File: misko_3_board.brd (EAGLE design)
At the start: 337 x 187 mm, 171 parts, among them IC1 ATMEGA1281-16AU, IC10 ORG1510-MK4, IC11 TPS3808G33DBVT, IC12 LTC4425, IC13 RN-42, IC14 ADXL345, IC15 74HCT1G32, IC16 FM25W256-SOIC, IC17 MICROSD_SPI_MODE, IC18 FH12-30S-0.5SH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

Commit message: - corrected too big spatial dimensions (took 1mm off), rerouted what needed to be rerouted, ERC & DRC are error free
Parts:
- moved CONN13 139.2 mm to (216.0, 13.0)
- moved LED1 139.2 mm to (210.0, 17.0)
- moved LED2 139.2 mm to (210.0, 13.5)
- moved LED5 139.2 mm to (225.5, 16.8)
- moved LED6 139.2 mm to (225.5, 13.5)
- moved R41 139.2 mm to (229.5, 13.5)
- moved R50 139.2 mm to (220.2, 13.5)
- moved S4 139.2 mm to (225.5, 8.50)
- moved S5 139.2 mm to (207.5, 8.50)
- moved C1 131.7 mm to (108.5, 32.6)
- moved C10 131.7 mm to (164.5, 2.50)
- moved C12 131.7 mm to (131.7, 23.5)
- moved C15 131.7 mm to (106.5, 8.50)
- moved C16 131.7 mm to (122.5, 23.5)
- moved C2 131.7 mm to (150.5, 21.0)
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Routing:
- net VUSB: track 47.1 -> 12.1 mm, vias 0 -> 1
- net RESET: track 167.0 -> 163.8 mm
- net VCC: track 458.7 -> 457.2 mm
- net GSM_ANT: track 11.0 -> 10.4 mm
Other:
- board size 337 x 187 mm -> 233 x 140 mm
- board text added: "Miško v.1"
- board text removed: "Miško"

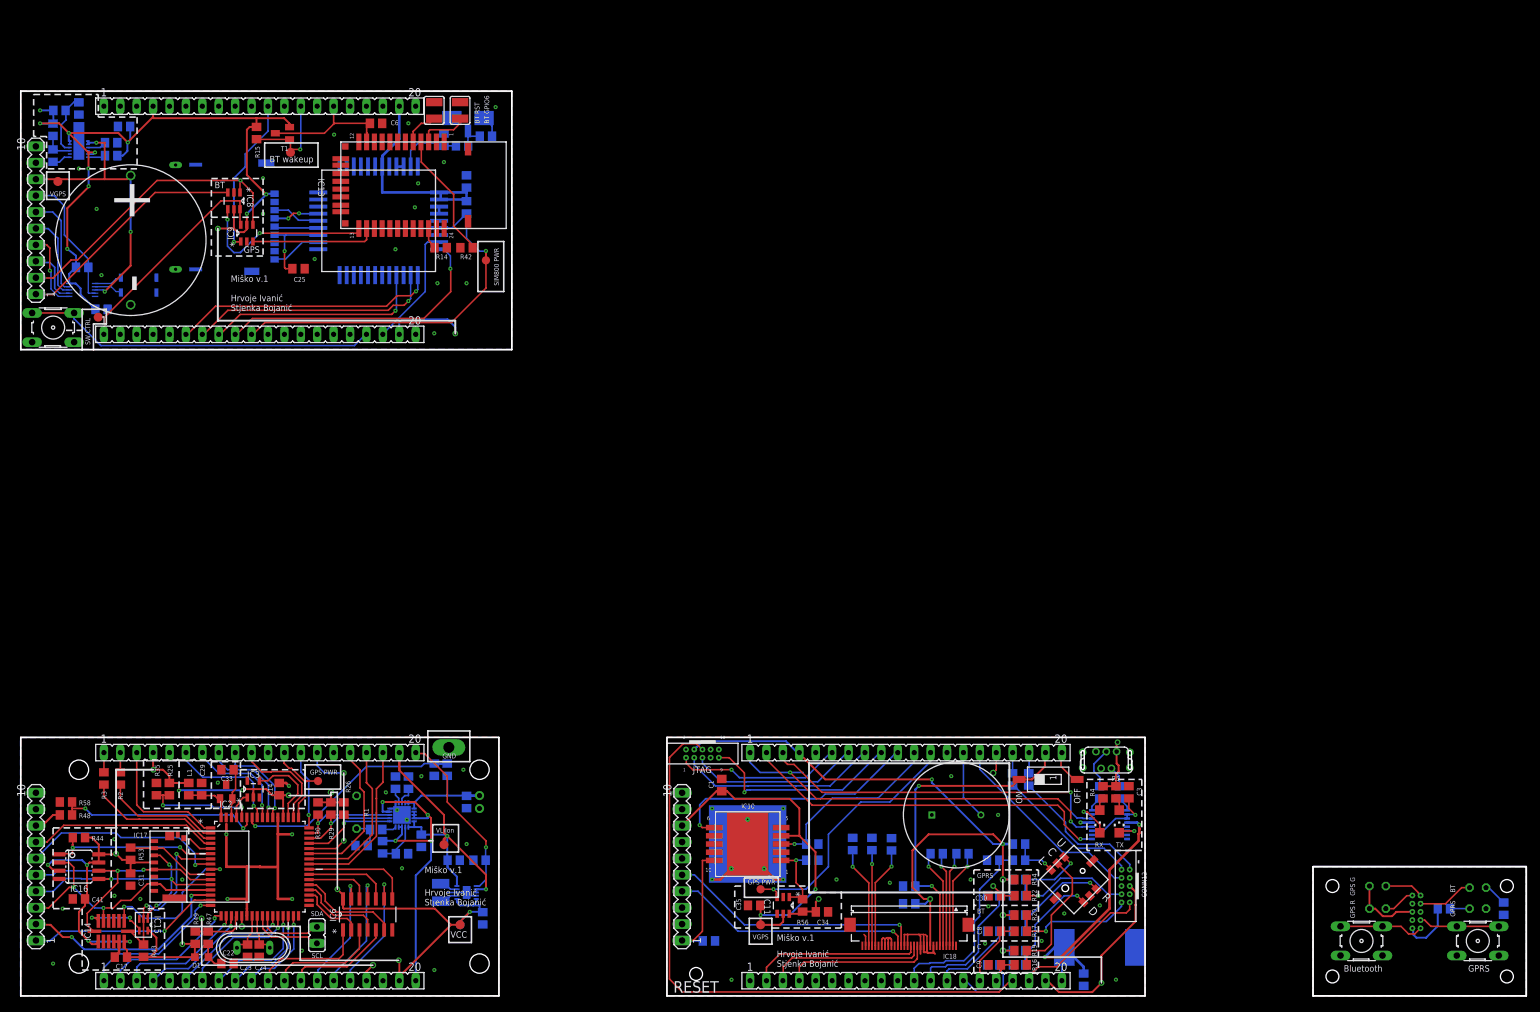
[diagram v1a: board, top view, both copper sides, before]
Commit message: - panelized, added fiducial marks
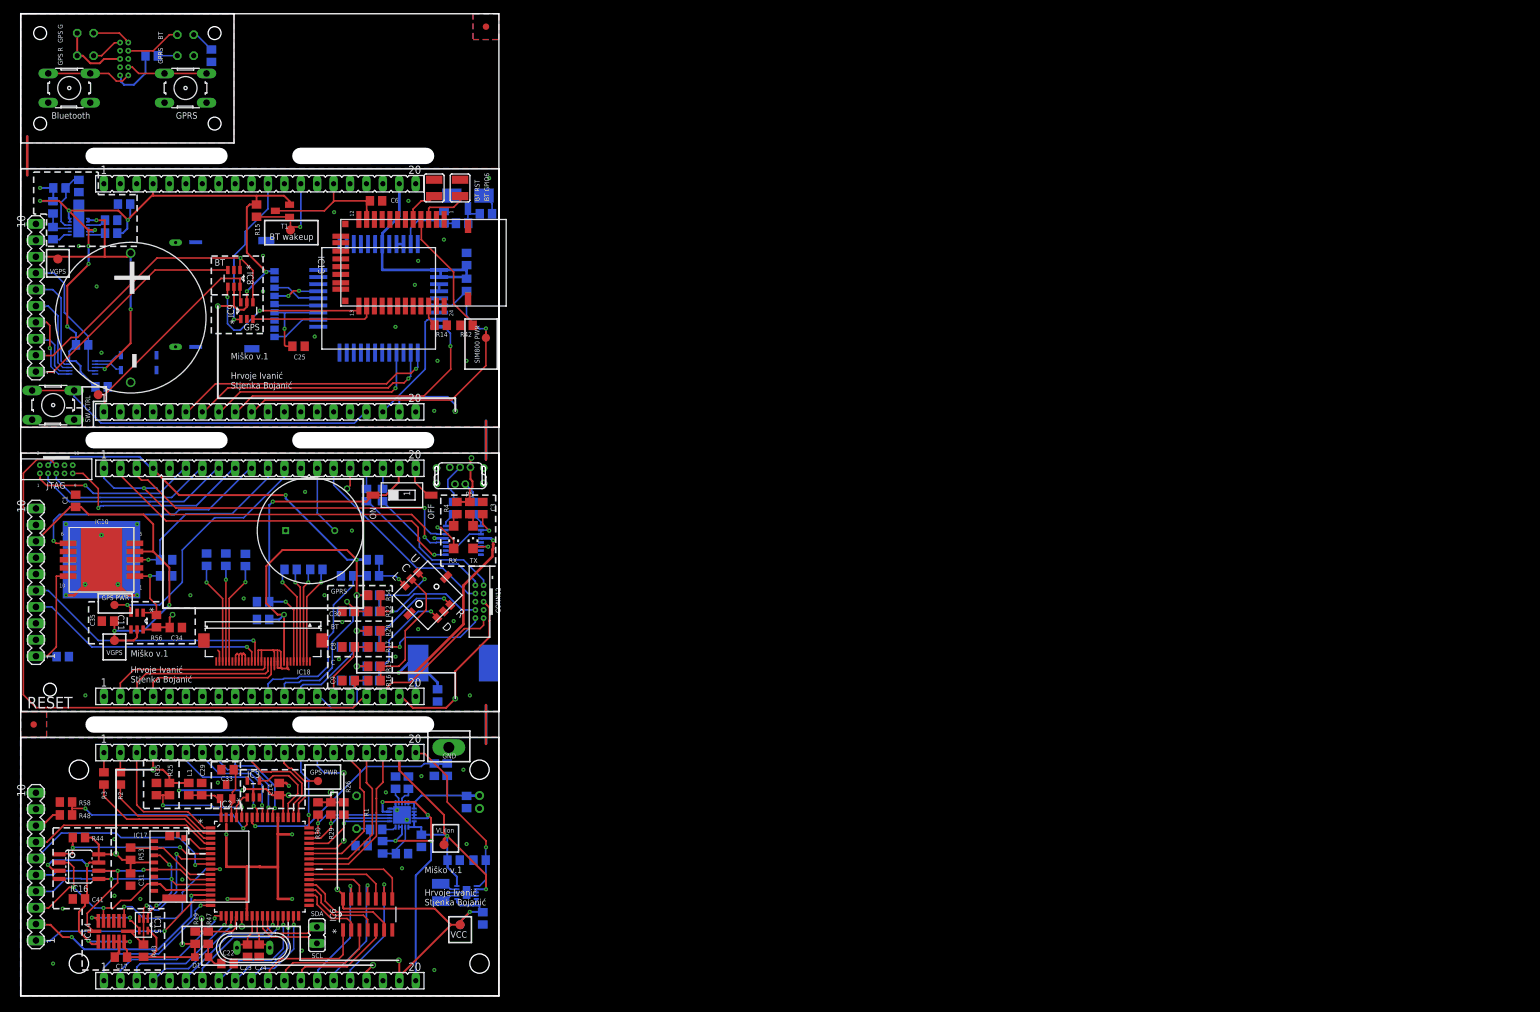
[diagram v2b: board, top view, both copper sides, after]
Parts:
- added U$2, U$3: FIDUCIAL, adafruit:FIDUCIAL_1MM
- moved CONN13 239.6 mm to (16.0, 145.0)
- moved LED1 239.6 mm to (10.0, 149.0)
- moved LED2 239.6 mm to (10.0, 145.5)
- moved LED5 239.6 mm to (25.5, 148.8)
- moved LED6 239.6 mm to (25.5, 145.5)
- moved R41 239.6 mm to (29.5, 145.5)
- moved R50 239.6 mm to (20.2, 145.5)
- moved S4 239.6 mm to (25.5, 140.5)
- moved S5 239.6 mm to (7.50, 140.5)
- moved C1 109.3 mm to (8.49, 76.6)
- moved C10 109.3 mm to (64.5, 46.5)
- moved C15 109.3 mm to (6.50, 52.5)
- moved C16 109.3 mm to (22.5, 67.5)
- moved C2 109.3 mm to (50.5, 65.0)
- moved C3 109.3 mm to (71.5, 75.5)
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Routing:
- net GND: track 95.3 -> 131.3 mm
- net VCC: track 457.2 -> 456.7 mm
- added copper zone on layer 1, net N$1
- added copper zone on layer 16, net N$2
- added copper zone on layer 16, net N$3
- added copper zone on layer 1, net N$4
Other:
- board size 233 x 140 mm -> 74 x 152 mm

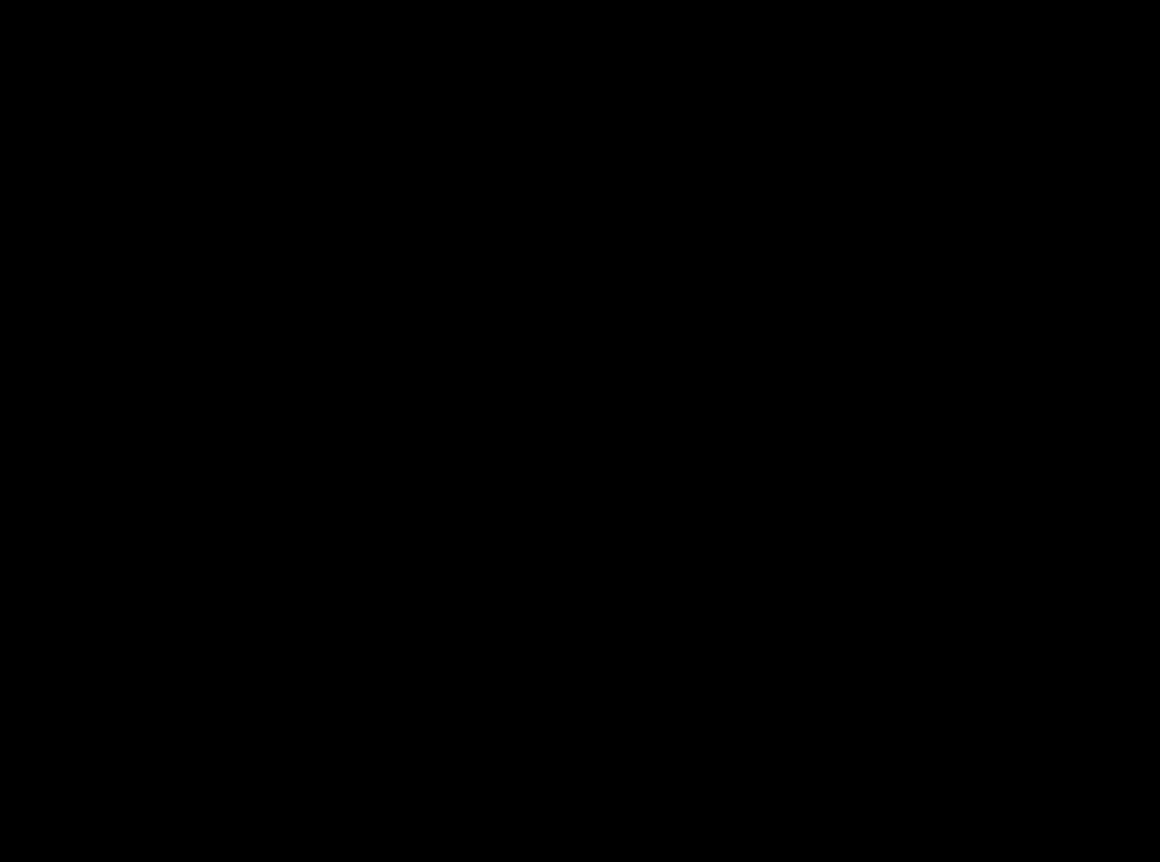
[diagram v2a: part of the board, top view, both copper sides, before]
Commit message: - implemented capacitor bank for support of solar panels (see adafruits solar charger)
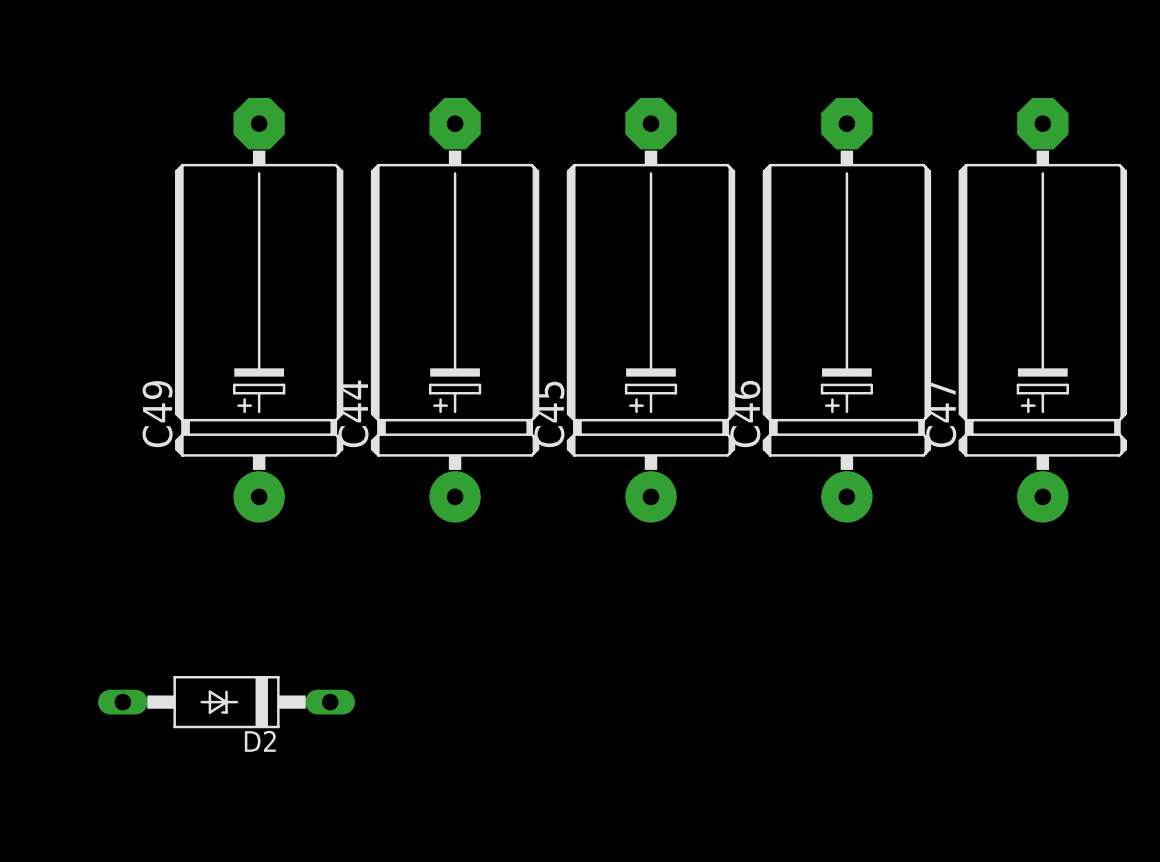
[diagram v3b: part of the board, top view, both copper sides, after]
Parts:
- added C44, C45, C46, C47, C49: 1000µF, rcl:E22-10
- added D2: (no value), eagle-ltspice:DIODE_F126Z12
- R48, R58: value 46k -> 150k
- renumbered U$2 to FI1, U$3 to FI2
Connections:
- new net N$6: C44.+, C45.+, C46.+, C47.+, C49.+, D2.C
- net 5V0: now also D2.A
- net GND: now also C44.-, C45.-, C46.-, C47.-, C49.-
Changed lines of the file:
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@@
 <attribute name="VALUE" x="31.54" y="8.365" size="1.27" layer="27" rot="R90"/>
 </element>
-<element name="R48" library="resistor" package="R0805" value="46k" x="7" y="28" smashed="yes">
+<element name="R48" library="resistor" package="R0805" value="150k" x="7" y="28" smashed="yes">
 <attribute name="NAME" x="9" y="27.5" size="0.75" layer="25"/>
 <attribute name="VALUE" x="6.365" y="25.46" size="1.27" layer="27"/>
@@
 <attribute name="VALUE" x="37.31" y="68.73" size="1.27" layer="28" rot="MR270"/>
 </element>
-<element name="R58" library="resistor" package="R0805" value="46k" x="7" y="30" smashed="yes" rot="R180">
+<element name="R58" library="resistor" package="R0805" value="150k" x="7" y="30" smashed="yes" rot="R180">
 <attribute name="NAME" x="9" y="29.5" size="0.75" layer="25"/>
 <attribute name="VALUE" x="7.635" y="32.54" size="1.27" layer="27" rot="R180"/>
@@
 <attribute name="VALUE" x="18.46" y="58.635" size="1.27" layer="27" rot="R270"/>
 </element>
-<element name="U$2" library="adafruit" package="FIDUCIAL_1MM" value="FIDUCIAL" x="2" y="42"/>
-<element name="U$3" library="adafruit" package="FIDUCIAL_1MM" value="FIDUCIAL" x="72" y="150"/>
+<element name="FI1" library="adafruit" package="FIDUCIAL_1MM" value="FIDUCIAL" x="2" y="42"/>
+<element name="FI2" library="adafruit" package="FIDUCIAL_1MM" value="FIDUCIAL" x="72" y="150"/>
+<element name="C49" library="rcl" package="E22-10" value="1000µF" x="99" y="34" rot="R90"/>
+<element name="C44" library="rcl" package="E22-10" value="1000µF" x="111" y="34" rot="R90"/>
+<element name="C45" library="rcl" package="E22-10" value="1000µF" x="123" y="34" rot="R90"/>
+<element name="C46" library="rcl" package="E22-10" value="1000µF" x="135" y="34" rot="R90"/>
+<element name="C47" library="rcl" package="E22-10" value="1000µF" x="147" y="34" rot="R90"/>
+<element name="D2" library="eagle-ltspice" package="DIODE_F126Z12" value="" x="97" y="10" rot="R180">
+<attribute name="SPICEMODEL" value="NONE" x="97" y="10" size="1.778" layer="27" rot="R180" display="off"/>
+<attribute name="SPICEPREFIX" value="D" x="97" y="10" size="1.778" layer="27" rot="R180" display="off"/>
+<attribute name="SPICETYPE" value="diode" x="97" y="10" size="1.778" layer="27" rot="R180" display="off"/>
+</element>
 </elements>
 <signals>
@@
 <wire x1="73.1" y1="70.5" x2="73.1" y2="69.84054375" width="0.4" layer="1"/>
 <wire x1="73.1" y1="69.84054375" x2="73.1082" y2="69.83234375" width="0.4" layer="1"/>
+<contactref element="D2" pad="A"/>
 <wire x1="71.2178" y1="70.8175" x2="61.12" y2="90.38" width="0" layer="19" extent="16-16"/>
 <wire x1="61" y1="30" x2="61.13" y2="46.35" width="0" layer="19" extent="1-1"/>
+<wire x1="90.65" y1="10" x2="63.5" y2="21" width="0" layer="19" extent="16-16"/>
 </signal>
 <signal name="MENU_LEFT_BUTTON_PIN" class="2">
@@
 <wire x1="72.94" y1="122.63" x2="71.71" y2="123.86" width="0.25" layer="16"/>
 <wire x1="72" y1="45" x2="72" y2="39" width="0.4" layer="1"/>
-<wire x1="59.75" y1="27.25" x2="59" y2="28" width="0" layer="19" extent="16-16"/>
-<wire x1="49.55" y1="48.8" x2="49.8" y2="48.8" width="0" layer="19" extent="1-16"/>
-<wire x1="49.55" y1="59.5" x2="49.8" y2="59.5" width="0" layer="19" extent="1-16"/>
-<wire x1="8.2612" y1="89.1694" x2="8.04" y2="82.13" width="0" layer="19" extent="1-1"/>
-<wire x1="22.2488" y1="138.2394" x2="23.02" y2="125.69" width="0" layer="19" extent="1-1"/>
 <wire x1="72" y1="45" x2="72" y2="39" width="0.4" layer="16"/>
 <wire x1="72" y1="89" x2="72" y2="83" width="0.4" layer="16"/>
@@
 <wire x1="1" y1="133" x2="1" y2="127" width="0.4" layer="1"/>
 <wire x1="1" y1="133" x2="1" y2="127" width="0.4" layer="16"/>
+<contactref element="C49" pad="-"/>
+<contactref element="C44" pad="-"/>
+<contactref element="C45" pad="-"/>
+<contactref element="C46" pad="-"/>
+<contactref element="C47" pad="-"/>
+<wire x1="135" y1="45.43" x2="147" y2="45.43" width="0" layer="19" extent="1-1"/>
+<wire x1="123" y1="45.43" x2="135" y2="45.43" width="0" layer="19" extent="1-1"/>
+<wire x1="111" y1="45.43" x2="123" y2="45.43" width="0" layer="19" extent="1-1"/>
+<wire x1="99" y1="45.43" x2="111" y2="45.43" width="0" layer="19" extent="1-1"/>
+<wire x1="72" y1="39" x2="99" y2="45.43" width="0" layer="19" extent="16-16"/>
+<wire x1="49.55" y1="48.8" x2="49.8" y2="48.8" width="0" layer="19" extent="1-16"/>
+<wire x1="49.55" y1="59.5" x2="49.8" y2="59.5" width="0" layer="19" extent="1-16"/>
+<wire x1="59" y1="28" x2="59.75" y2="27.25" width="0" layer="19" extent="16-16"/>
 </signal>
 <signal name="GPRS_LED" class="2">
@@
 </polygon>
 </signal>
+<signal name="N$6">
+<contactref element="C49" pad="+"/>
+<contactref element="C44" pad="+"/>
+<contactref element="C45" pad="+"/>
+<contactref element="C46" pad="+"/>
+<contactref element="C47" pad="+"/>
+<contactref element="D2" pad="C"/>
+<wire x1="135" y1="22.57" x2="147" y2="22.57" width="0" layer="19" extent="1-1"/>
+<wire x1="123" y1="22.57" x2="135" y2="22.57" width="0" layer="19" extent="1-1"/>
+<wire x1="111" y1="22.57" x2="123" y2="22.57" width="0" layer="19" extent="1-1"/>
+<wire x1="99" y1="22.57" x2="111" y2="22.57" width="0" layer="19" extent="1-1"/>
+<wire x1="103.35" y1="10" x2="99" y2="22.57" width="0" layer="19" extent="1-1"/>
+</signal>
 </signals>
